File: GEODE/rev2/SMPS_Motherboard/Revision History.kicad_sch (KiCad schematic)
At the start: 0 parts

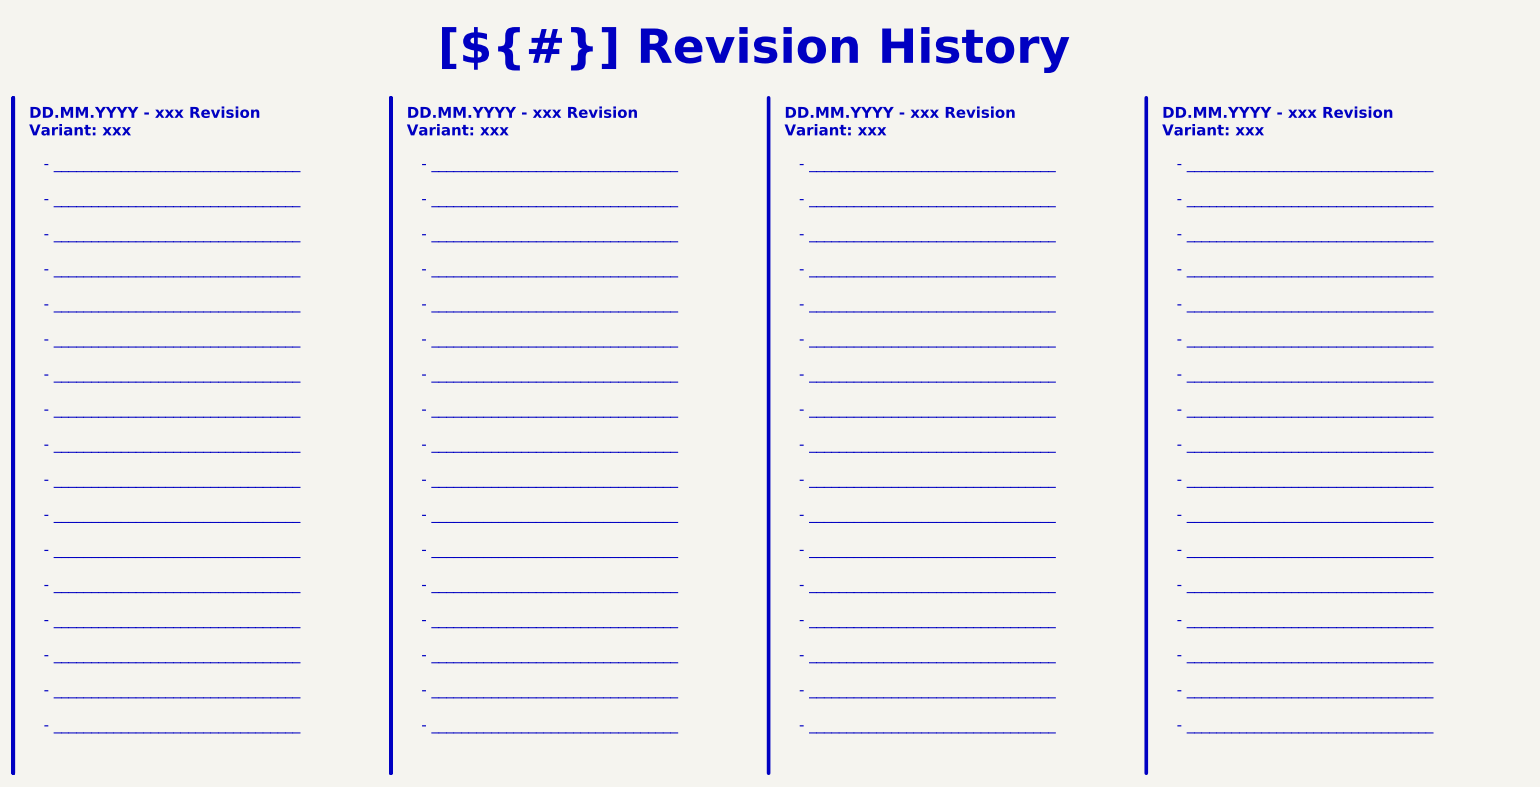
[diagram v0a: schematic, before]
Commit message: changed connectors, removed can, added fuse, disconnected EXTVCC in power generation
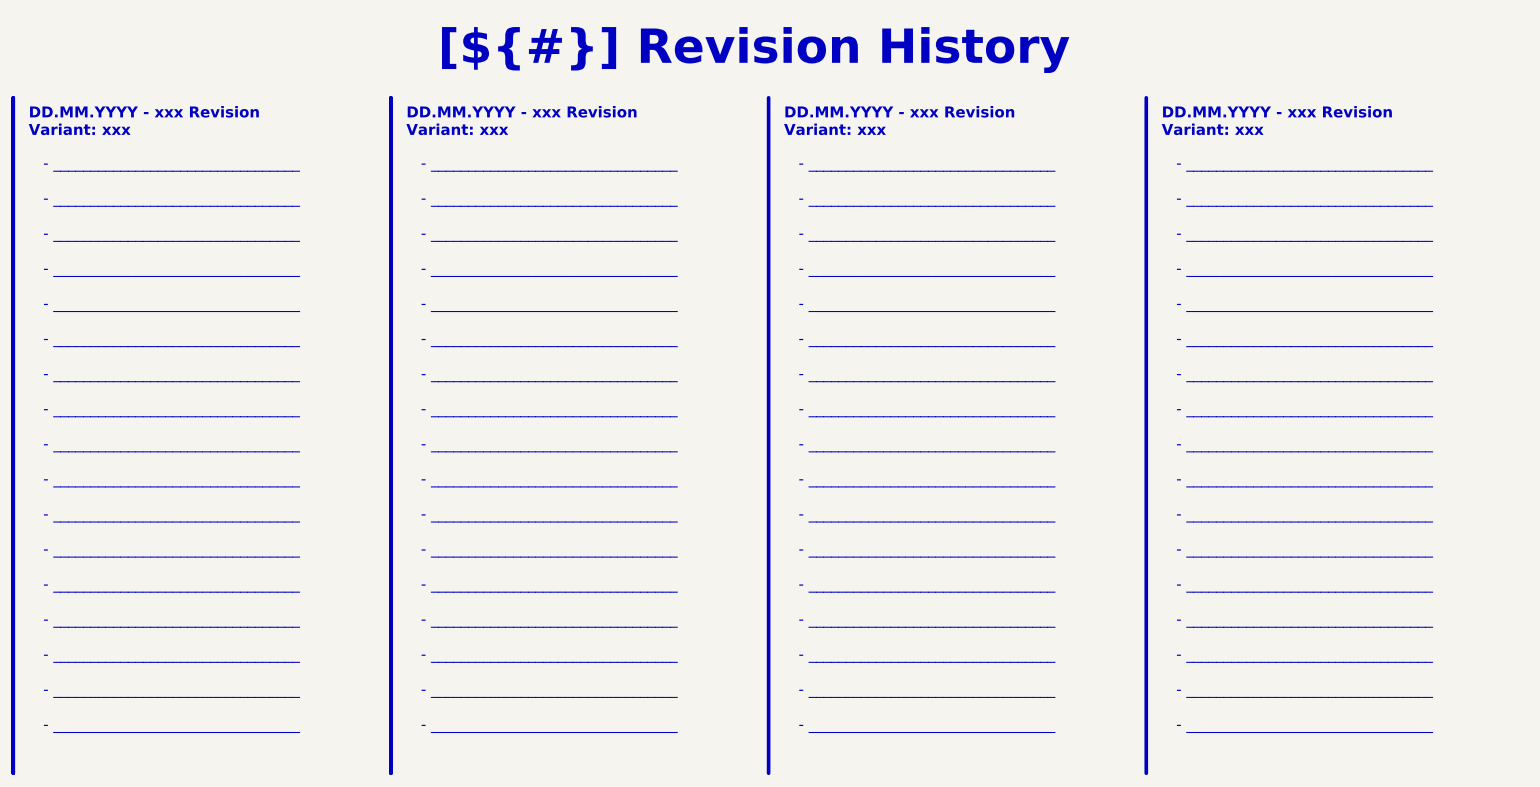
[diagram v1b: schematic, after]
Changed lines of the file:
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@@
 (kicad_sch
-	(version 20231120)
+	(version 20250114)
 	(generator "eeschema")
-	(generator_version "8.0")
+	(generator_version "9.0")
 	(paper "A4")
 	(title_block
@@
 		(company "${COMPANY}")
 	)
-	(polyline
-		(pts
-			(xy 19.05 31.75) (xy 19.05 149.86)
-		)
-		(stroke
-			(width 0.635)
-			(type default)
-			(color 0 0 0 1)
-		)
-	)
-	(polyline
-		(pts
-			(xy 85.09 31.75) (xy 85.09 149.86)
-		)
-		(stroke
-			(width 0.635)
-			(type default)
-			(color 0 0 0 1)
-		)
-	)
-	(polyline
-		(pts
-			(xy 85.09 31.75) (xy 85.09 149.86)
-		)
-		(stroke
-			(width 0.635)
-			(type default)
-			(color 0 0 0 1)
-		)
-	)
-	(polyline
-		(pts
-			(xy 151.13 31.75) (xy 151.13 149.86)
-		)
-		(stroke
-			(width 0.635)
-			(type default)
-			(color 0 0 0 1)
-		)
-	)
-	(polyline
-		(pts
-			(xy 19.05 31.75) (xy 19.05 149.86)
-		)
-		(stroke
-			(width 0.635)
-			(type default)
-			(color 0 0 0 1)
-		)
-	)
-	(polyline
-		(pts
-			(xy 217.17 31.75) (xy 217.17 149.86)
-		)
-		(stroke
-			(width 0.635)
-			(type default)
-			(color 0 0 0 1)
-		)
-	)
 	(text_box "- _________________________________\n\n- _________________________________\n\n- _________________________________\n\n- _________________________________\n\n- _________________________________\n\n- _________________________________\n\n- _________________________________\n\n- _________________________________\n\n- _________________________________\n\n- _________________________________\n\n- _________________________________\n\n- _________________________________\n\n- _________________________________\n\n- _________________________________\n\n- _________________________________\n\n- _________________________________\n\n- _________________________________"
 		(exclude_from_sim no)
 		(at 220.98 40.64 0)
 		(size 58.42 115.57)
+		(margins 1.4287 1.4287 1.4287 1.4287)
 		(stroke
 			(width -0.0001)
@@
 		(at 86.36 31.75 0)
 		(size 57.15 7.62)
+		(margins 1.4287 1.4287 1.4287 1.4287)
 		(stroke
 			(width -0.0001)
@@
 		(at 80.01 16.51 0)
 		(size 137.16 12.7)
+		(margins 4.4999 4.4999 4.4999 4.4999)
 		(stroke
 			(width -0.0001)
@@
 		(at 152.4 31.75 0)
 		(size 57.15 7.62)
+		(margins 1.4287 1.4287 1.4287 1.4287)
 		(stroke
 			(width -0.0001)
@@
 		(at 22.86 40.64 0)
 		(size 58.42 115.57)
+		(margins 1.4287 1.4287 1.4287 1.4287)
 		(stroke
 			(width -0.0001)
@@
 		(at 154.94 40.64 0)
 		(size 58.42 115.57)
+		(margins 1.4287 1.4287 1.4287 1.4287)
 		(stroke
 			(width -0.0001)
@@
 		(at 20.32 31.75 0)
 		(size 57.15 7.62)
+		(margins 1.4287 1.4287 1.4287 1.4287)
 		(stroke
 			(width -0.0001)
@@
 		(at 88.9 40.64 0)
 		(size 58.42 115.57)
+		(margins 1.4287 1.4287 1.4287 1.4287)
 		(stroke
 			(width -0.0001)
@@
 		(at 218.44 31.75 0)
 		(size 57.15 7.62)
-		(stroke
-			(width -0.0001)
-			(type default)
-		)
-		(fill
-			(type none)
-		)
-		(effects
-			(font
-				(face "Arial")
-				(size 1.905 1.905)
-				(thickness 0.254)
-				(bold yes)
-			)
-			(justify left top)
-		)
-	)
+		(margins 1.4287 1.4287 1.4287 1.4287)
+		(stroke
+			(width -0.0001)
+			(type default)
+		)
+		(fill
+			(type none)
+		)
+		(effects
+			(font
+				(face "Arial")
+				(size 1.905 1.905)
+				(thickness 0.254)
+				(bold yes)
+			)
+			(justify left top)
+		)
+	)
+	(polyline
+		(pts
+			(xy 19.05 31.75) (xy 19.05 149.86)
+		)
+		(stroke
+			(width 0.635)
+			(type default)
+			(color 0 0 0 1)
+		)
+	)
+	(polyline
+		(pts
+			(xy 85.09 31.75) (xy 85.09 149.86)
+		)
+		(stroke
+			(width 0.635)
+			(type default)
+			(color 0 0 0 1)
+		)
+	)
+	(polyline
+		(pts
+			(xy 85.09 31.75) (xy 85.09 149.86)
+		)
+		(stroke
+			(width 0.635)
+			(type default)
+			(color 0 0 0 1)
+		)
+	)
+	(polyline
+		(pts
+			(xy 151.13 31.75) (xy 151.13 149.86)
+		)
+		(stroke
+			(width 0.635)
+			(type default)
+			(color 0 0 0 1)
+		)
+	)
+	(polyline
+		(pts
+			(xy 19.05 31.75) (xy 19.05 149.86)
+		)
+		(stroke
+			(width 0.635)
+			(type default)
+			(color 0 0 0 1)
+		)
+	)
+	(polyline
+		(pts
+			(xy 217.17 31.75) (xy 217.17 149.86)
+		)
+		(stroke
+			(width 0.635)
+			(type default)
+			(color 0 0 0 1)
+		)
+	)
